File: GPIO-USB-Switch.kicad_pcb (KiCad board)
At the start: 4 copper layers, 20 x 38 mm, 15 parts, among them J1 GPIO_OUT, J2 USB3.0-Type-A_Male, J3 USB3.0-Type-A_Female, Q1 2N7002, Q2 DMG2301L

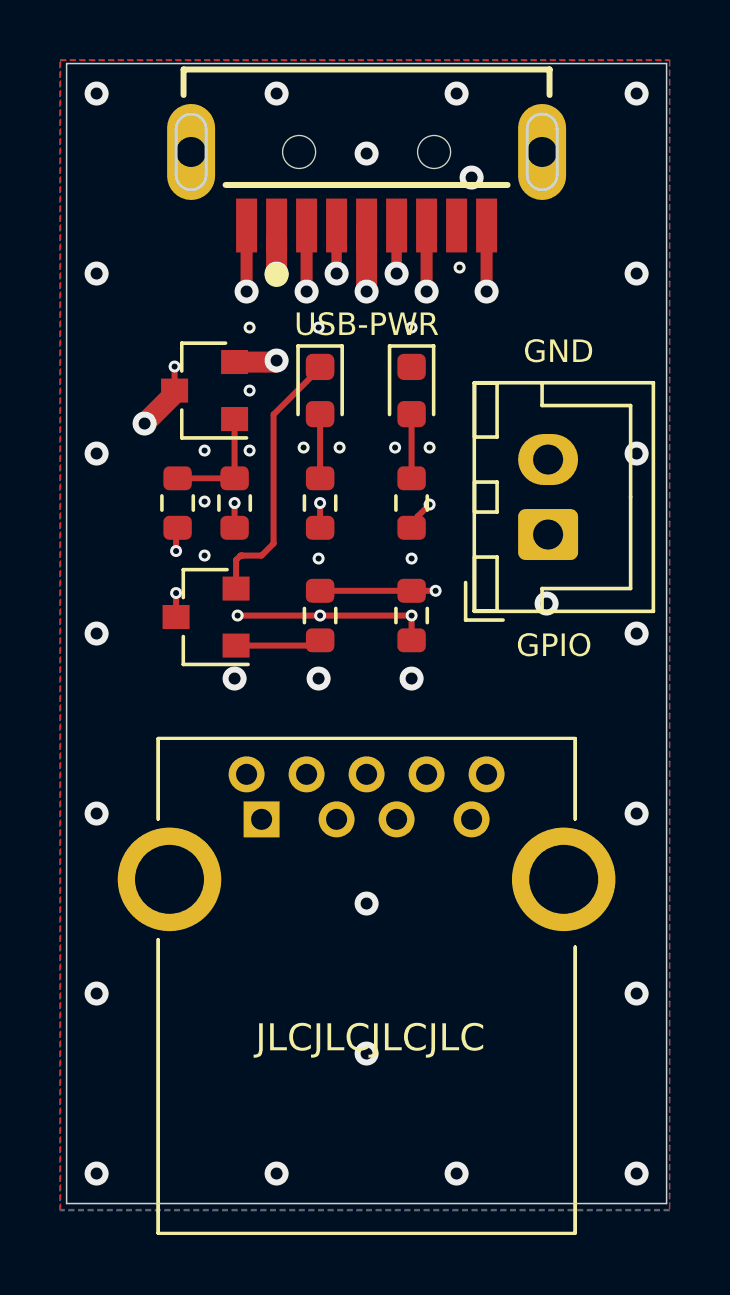
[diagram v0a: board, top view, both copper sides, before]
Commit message: changed minimum via size to 0.2mm/0.45mm
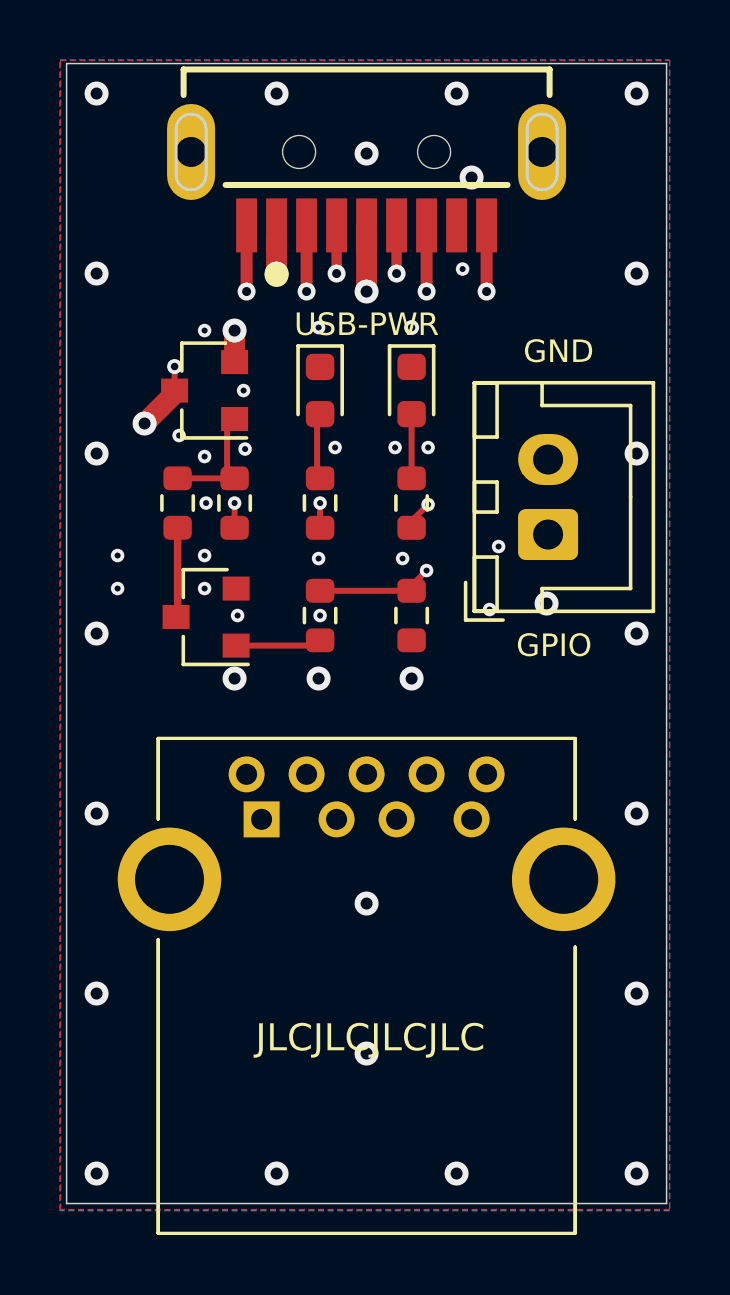
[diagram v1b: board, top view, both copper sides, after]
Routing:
- net GND: track 15.5 -> 0.00 mm, vias 44 -> 48
- net VBUS: track 18.0 -> 17.3 mm
- net Net-(Q1-Pad3): track 2.92 -> 3.10 mm, vias 2 -> 0
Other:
- rule via_min_size: 0.4 -> 0.45
